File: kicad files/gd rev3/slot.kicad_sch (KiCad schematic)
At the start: 11 parts, among them J10 Apple_II_Slot, J11 Slot-Only Sigs, J12 -5V, SW2 DEV, SW3 IOSEL, U12 Slotmaker, U13 74HCT245

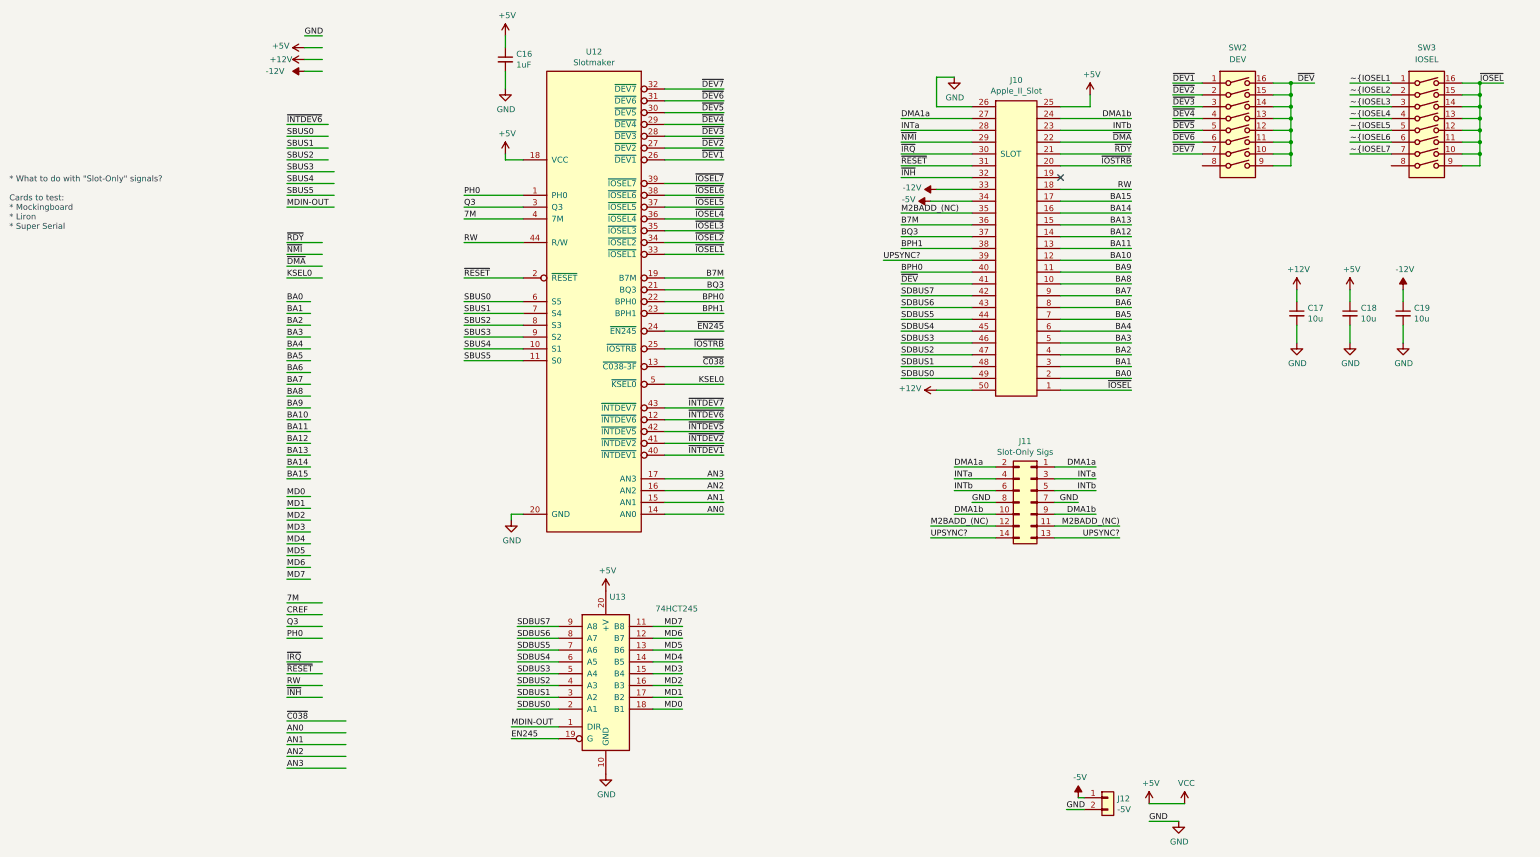
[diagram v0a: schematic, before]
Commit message: initial slot/io breakout sheet labels
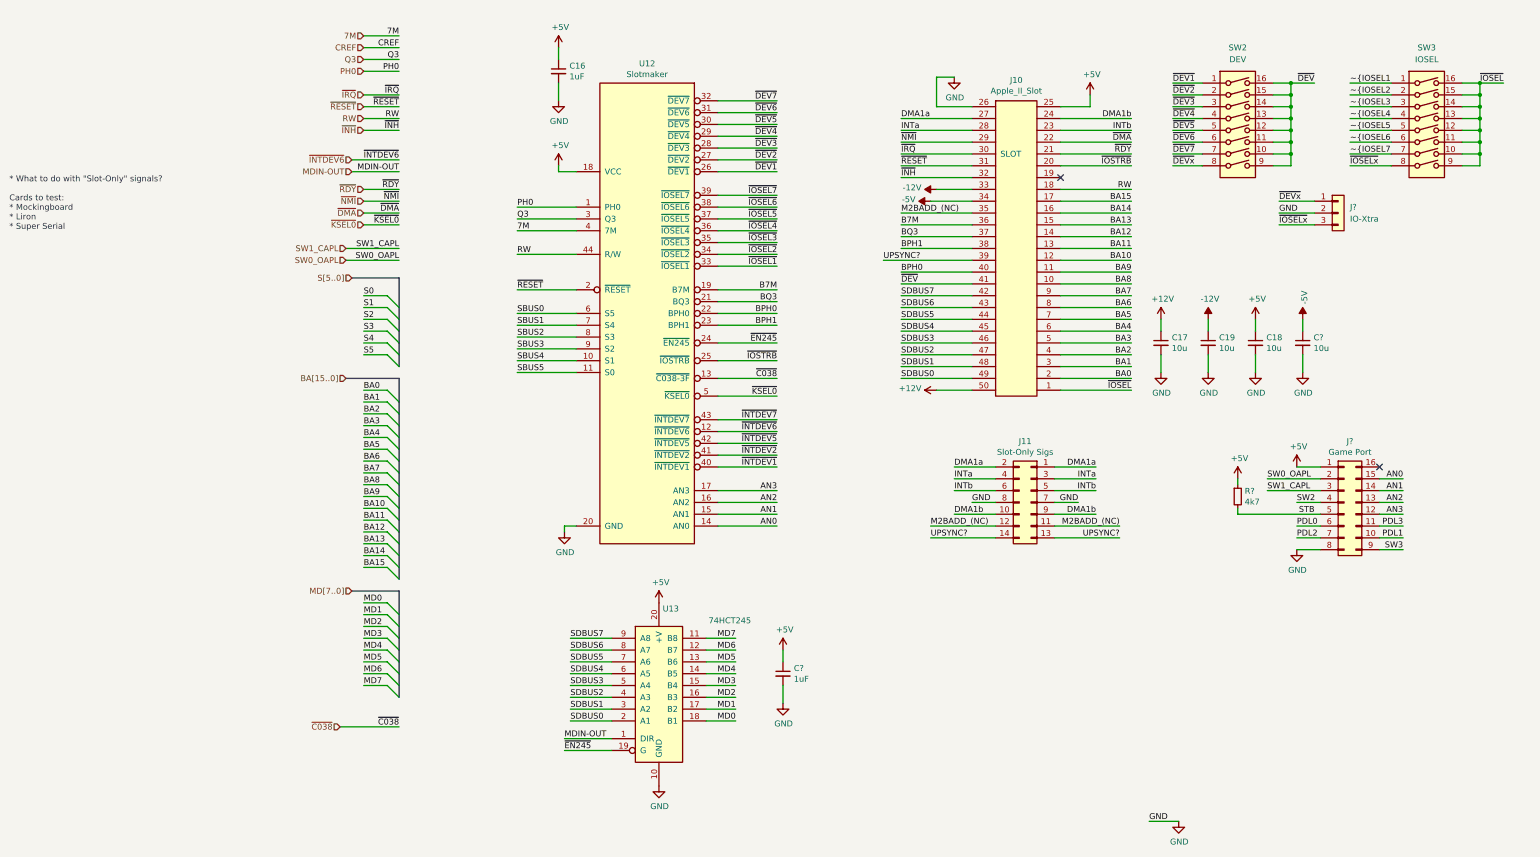
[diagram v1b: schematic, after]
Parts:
- removed J12: -5V, My Libraries:PinHeader_1x02_P2.54mm_Vertical-LOCK, symbol Connector_Generic:Conn_01x02
- added C?: 10u, Capacitor_SMD:C_0805_2012Metric, symbol My_Library:C_0805
- added C?: 1uF, Capacitor_SMD:C_0805_2012Metric, symbol My_Library:C_0805
- added J?: IO-Xtra, symbol Connector_Generic:Conn_01x03
- added J?: Game Port, Package_DIP:DIP-16_W7.62mm_Socket, symbol Connector_Generic:Conn_02x08_Counter_Clockwise
- added R?: 4k7, Resistor_SMD:R_0805_2012Metric, symbol My_Library:R_0805
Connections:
- net EN245 is gone; now on net ~{EN245}: U13.19 (G)
- net +5V: now also C?.1, J?.1 (Pin_1), R?.1
- net -5V: now also C?.1
- net AN0: now also J?.15 (Pin_15)
- net AN1: now also J?.14 (Pin_14)
- net AN2: now also J?.13 (Pin_13)
- net AN3: now also J?.12 (Pin_12)
- net GND: now also C?.2, C?.2, J?.2 (Pin_2), J?.8 (Pin_8)
- net ~{DEVx}: now reaches SW2.8
- net ~{DEVx}: now also J?.1 (Pin_1)
- net ~{IOSELx}: now reaches SW3.8
- net ~{IOSELx}: now also J?.3 (Pin_3)
- net KSEL0 renamed ~{KSEL0}
- new net PDL0: J?.6 (Pin_6)
- new net PDL1: J?.10 (Pin_10)
- new net PDL2: J?.7 (Pin_7)
- new net PDL3: J?.11 (Pin_11)
- new net STB: J?.5 (Pin_5), R?.2
- new net SW0_OAPL: J?.2 (Pin_2)
- new net SW1_CAPL: J?.3 (Pin_3)
- new net SW2: J?.4 (Pin_4)
- new net SW3: J?.9 (Pin_9)
- no-connect marks 1 -> 2
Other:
- note added: "~{}"
- title: (none) -> Slotmaker and Game DIP
- moved on the sheet: C16, C17, C18, C19, U12, U13

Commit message: update to pcb, minor updates to component placements
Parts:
- J9: renamed from J?; footprint (none) -> Connector_PinHeader_2.54mm:PinHeader_1x03_P2.54mm_Vertical
- gave numbers to parts that had none: 4
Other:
- moved on the sheet: J9
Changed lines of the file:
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@@
     (stroke (width 0) (type default) (color 0 0 0 0))
   )
-  (wire (pts (xy 231.14 60.96) (xy 238.76 60.96))
+  (wire (pts (xy 232.41 64.77) (xy 240.03 64.77))
     (stroke (width 0) (type default) (color 0 0 0 0))
   )
@@
     (stroke (width 0) (type default) (color 0 0 0 0))
   )
-  (wire (pts (xy 231.14 58.42) (xy 238.76 58.42))
+  (wire (pts (xy 232.41 62.23) (xy 240.03 62.23))
     (stroke (width 0) (type default) (color 0 0 0 0))
   )
@@
     (stroke (width 0) (type default) (color 0 0 0 0))
   )
-  (wire (pts (xy 231.14 63.5) (xy 238.76 63.5))
+  (wire (pts (xy 232.41 67.31) (xy 240.03 67.31))
     (stroke (width 0) (type default) (color 0 0 0 0))
   )
@@
     (effects (font (size 1.27 1.27)) (justify right bottom))
   )
-  (label "GND" (at 231.14 60.96 0)
+  (label "GND" (at 232.41 64.77 0)
     (effects (font (size 1.27 1.27)) (justify left bottom))
   )
@@
     (effects (font (size 1.27 1.27)) (justify left bottom))
   )
-  (label "~{IOSELx}" (at 231.14 63.5 0)
+  (label "~{IOSELx}" (at 232.41 67.31 0)
     (effects (font (size 1.27 1.27)) (justify left bottom))
   )
@@
     (effects (font (size 1.27 1.27)) (justify left bottom))
   )
-  (label "~{DEVx}" (at 231.14 58.42 0)
+  (label "~{DEVx}" (at 232.41 62.23 0)
     (effects (font (size 1.27 1.27)) (justify left bottom))
   )
@@
   (symbol (lib_id "power:GND") (at 234.95 133.35 0) (unit 1)
     (in_bom yes) (on_board yes)
-    (property "Reference" "#PWR?" (id 0) (at 234.95 139.7 0)
+    (property "Reference" "#PWR0217" (id 0) (at 234.95 139.7 0)
       (effects (font (size 1.27 1.27)) hide)
     )
@@
   (symbol (lib_id "power:+5V") (at 222.25 118.11 0) (unit 1)
     (in_bom yes) (on_board yes)
-    (property "Reference" "#PWR?" (id 0) (at 222.25 121.92 0)
+    (property "Reference" "#PWR0208" (id 0) (at 222.25 121.92 0)
       (effects (font (size 1.27 1.27)) hide)
     )
@@
   (symbol (lib_id "My_Library:C_0805") (at 236.22 88.9 0) (unit 1)
     (in_bom yes) (on_board yes)
-    (property "Reference" "C?" (id 0) (at 238.5568 87.7316 0)
+    (property "Reference" "C56" (id 0) (at 238.5568 87.7316 0)
       (effects (font (size 1.27 1.27)) (justify left))
     )
@@
     (pin "1")
   )
-  (symbol (lib_id "Connector_Generic:Conn_01x03") (at 243.84 60.96 0) (unit 1)
+  (symbol (lib_id "Connector_Generic:Conn_01x03") (at 245.11 64.77 0) (unit 1)
     (in_bom yes) (on_board yes) (fields_autoplaced)
-    (property "Reference" "J?" (id 0) (at 246.38 59.6899 0)
+    (property "Reference" "J9" (id 0) (at 247.65 63.4999 0)
       (effects (font (size 1.27 1.27)) (justify left))
     )
-    (property "Value" "IO-Xtra" (id 1) (at 246.38 62.2299 0)
+    (property "Value" "IO-Xtra" (id 1) (at 247.65 66.0399 0)
       (effects (font (size 1.27 1.27)) (justify left))
     )
-    (property "Footprint" "" (id 2) (at 243.84 60.96 0)
-      (effects (font (size 1.27 1.27)) hide)
-    )
-    (property "Datasheet" "~" (id 3) (at 243.84 60.96 0)
+    (property "Footprint" "Connector_PinHeader_2.54mm:PinHeader_1x03_P2.54mm_Vertical" (id 2) (at 245.11 64.77 0)
+      (effects (font (size 1.27 1.27)) hide)
+    )
+    (property "Datasheet" "~" (id 3) (at 245.11 64.77 0)
       (effects (font (size 1.27 1.27)) hide)
     )
@@
   (symbol (lib_id "power:GND") (at 236.22 95.25 0) (unit 1)
     (in_bom yes) (on_board yes)
-    (property "Reference" "#PWR?" (id 0) (at 236.22 101.6 0)
+    (property "Reference" "#PWR0176" (id 0) (at 236.22 101.6 0)
       (effects (font (size 1.27 1.27)) hide)
     )
@@
   (symbol (lib_id "power:+5V") (at 124.46 154.94 0) (unit 1)
     (in_bom yes) (on_board yes)
-    (property "Reference" "#PWR?" (id 0) (at 124.46 158.75 0)
+    (property "Reference" "#PWR0206" (id 0) (at 124.46 158.75 0)
       (effects (font (size 1.27 1.27)) hide)
     )
@@
   (symbol (lib_id "My_Library:C_0805") (at 124.46 160.02 0) (unit 1)
     (in_bom yes) (on_board yes)
-    (property "Reference" "C?" (id 0) (at 126.7968 158.8516 0)
+    (property "Reference" "C55" (id 0) (at 126.7968 158.8516 0)
       (effects (font (size 1.27 1.27)) (justify left))
     )
@@
   (symbol (lib_id "power:+5V") (at 234.95 115.57 0) (unit 1)
     (in_bom yes) (on_board yes)
-    (property "Reference" "#PWR?" (id 0) (at 234.95 119.38 0)
+    (property "Reference" "#PWR0209" (id 0) (at 234.95 119.38 0)
       (effects (font (size 1.27 1.27)) hide)
     )
@@
   (symbol (lib_id "My_Library:R_0805") (at 222.25 121.92 0) (unit 1)
     (in_bom yes) (on_board yes)
-    (property "Reference" "R?" (id 0) (at 223.7486 120.7516 0)
+    (property "Reference" "R20" (id 0) (at 223.7486 120.7516 0)
       (effects (font (size 1.27 1.27)) (justify left))
     )
@@
   (symbol (lib_id "power:-5V") (at 236.22 83.82 0) (unit 1)
     (in_bom yes) (on_board yes)
-    (property "Reference" "#PWR?" (id 0) (at 236.22 81.28 0)
+    (property "Reference" "#PWR0175" (id 0) (at 236.22 81.28 0)
       (effects (font (size 1.27 1.27)) hide)
     )
@@
   (symbol (lib_id "Connector_Generic:Conn_02x08_Counter_Clockwise") (at 245.11 123.19 0) (unit 1)
     (in_bom yes) (on_board yes)
-    (property "Reference" "J?" (id 0) (at 246.38 110.0582 0))
+    (property "Reference" "J12" (id 0) (at 246.38 110.0582 0))
     (property "Value" "Game Port" (id 1) (at 246.38 112.3696 0))
     (property "Footprint" "Package_DIP:DIP-16_W7.62mm_Socket" (id 2) (at 245.11 123.19 0)
@@
   (symbol (lib_id "power:GND") (at 124.46 166.37 0) (unit 1)
     (in_bom yes) (on_board yes)
-    (property "Reference" "#PWR?" (id 0) (at 124.46 172.72 0)
-      (effects (font (size 1.27 1.27)) hide)
-    )
+    (property "Reference" "#PWR0178" (id 0) (at 124.46 172.72 0)
+      (effects (font (size 1.27 1.27)) hide)
+    )

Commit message: ERC clean-up, wow, intern really messed up the symbols
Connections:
- net SBUS0 is gone; now on net S5: U12.6 (S5)
- net SBUS1 is gone; now on net S4: U12.7 (S4)
- net SBUS2 is gone; now on net S3: U12.8 (S3)
- net SBUS3 is gone; now on net S2: U12.9 (S2)
- net SBUS4 is gone; now on net S1: U12.10 (S1)
- net SBUS5 is gone; now on net S0: U12.11 (S0)
- net MDIN-OUT renamed MDI-MDO
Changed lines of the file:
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@@
-    (stroke (width 0) (type default) (color 0 0 0 0))
-  )
-  (wire (pts (xy 41.91 25.4) (xy 34.29 25.4))
     (stroke (width 0) (type default) (color 0 0 0 0))
   )
@@
     (effects (font (size 1.27 1.27)) (justify left bottom))
   )
+  (label "S1" (at 67.31 92.71 0)
+    (effects (font (size 1.27 1.27)) (justify left bottom))
+  )
   (label "MD7" (at 114.3 152.4 180)
     (effects (font (size 1.27 1.27)) (justify right bottom))
@@
     (effects (font (size 1.27 1.27)) (justify right bottom))
   )
-  (label "SBUS5" (at 67.31 95.25 0)
-    (effects (font (size 1.27 1.27)) (justify left bottom))
-  )
   (label "BA14" (at 34.29 134.62 0)
     (effects (font (size 1.27 1.27)) (justify left bottom))
@@
     (effects (font (size 1.27 1.27)) (justify right bottom))
   )
-  (label "CREF" (at 41.91 25.4 180)
-    (effects (font (size 1.27 1.27)) (justify right bottom))
-  )
   (label "SDBUS4" (at 149.86 86.36 0)
     (effects (font (size 1.27 1.27)) (justify left bottom))
@@
     (effects (font (size 1.27 1.27)) (justify right bottom))
   )
+  (label "S3" (at 67.31 87.63 0)
+    (effects (font (size 1.27 1.27)) (justify left bottom))
+  )
   (label "SDBUS6" (at 149.86 81.28 0)
     (effects (font (size 1.27 1.27)) (justify left bottom))
@@
     (effects (font (size 1.27 1.27)) (justify right bottom))
   )
+  (label "S2" (at 67.31 90.17 0)
+    (effects (font (size 1.27 1.27)) (justify left bottom))
+  )
   (label "RW" (at 41.91 40.64 180)
     (effects (font (size 1.27 1.27)) (justify right bottom))
@@
     (effects (font (size 1.27 1.27)) (justify left bottom))
   )
+  (label "S4" (at 67.31 85.09 0)
+    (effects (font (size 1.27 1.27)) (justify left bottom))
+  )
   (label "~{INTDEV6}" (at 123.19 107.95 180)
     (effects (font (size 1.27 1.27)) (justify right bottom))
@@
     (effects (font (size 1.27 1.27)) (justify right bottom))
   )
-  (label "MDIN-OUT" (at 41.91 52.07 180)
+  (label "MDI-MDO" (at 41.91 52.07 180)
     (effects (font (size 1.27 1.27)) (justify right bottom))
   )
@@
     (effects (font (size 1.27 1.27)) (justify right bottom))
   )
-  (label "MDIN-OUT" (at 77.47 173.99 0)
-    (effects (font (size 1.27 1.27)) (justify left bottom))
-  )
   (label "S2" (at 34.29 83.82 0)
     (effects (font (size 1.27 1.27)) (justify left bottom))
@@
     (effects (font (size 1.27 1.27)) (justify right bottom))
   )
-  (label "SBUS0" (at 67.31 82.55 0)
-    (effects (font (size 1.27 1.27)) (justify left bottom))
-  )
   (label "~{DEV1}" (at 208.28 33.02 0)
     (effects (font (size 1.27 1.27)) (justify left bottom))
@@
     (effects (font (size 1.27 1.27)) (justify left bottom))
   )
-  (label "SBUS3" (at 67.31 90.17 0)
-    (effects (font (size 1.27 1.27)) (justify left bottom))
-  )
   (label "~{DEVx}" (at 232.41 62.23 0)
     (effects (font (size 1.27 1.27)) (justify left bottom))
@@
     (effects (font (size 1.27 1.27)) (justify left bottom))
   )
-  (label "SBUS1" (at 67.31 85.09 0)
-    (effects (font (size 1.27 1.27)) (justify left bottom))
-  )
   (label "~{DEV}" (at 238.76 33.02 180)
     (effects (font (size 1.27 1.27)) (justify right bottom))
@@
     (effects (font (size 1.27 1.27)) (justify right bottom))
   )
+  (label "S5" (at 67.31 82.55 0)
+    (effects (font (size 1.27 1.27)) (justify left bottom))
+  )
   (label "~{INTDEV6}" (at 41.91 49.53 180)
     (effects (font (size 1.27 1.27)) (justify right bottom))
@@
     (effects (font (size 1.27 1.27)) (justify left bottom))
   )
-  (label "SBUS4" (at 67.31 92.71 0)
-    (effects (font (size 1.27 1.27)) (justify left bottom))
-  )
   (label "~{IOSTRB}" (at 199.39 50.8 180)
     (effects (font (size 1.27 1.27)) (justify right bottom))
@@
     (effects (font (size 1.27 1.27)) (justify right bottom))
   )
+  (label "MDI-MDO" (at 77.47 173.99 0)
+    (effects (font (size 1.27 1.27)) (justify left bottom))
+  )
   (label "~{IOSEL5" (at 246.38 43.18 0)
     (effects (font (size 1.27 1.27)) (justify left bottom))
@@
     (effects (font (size 1.27 1.27)) (justify left bottom))
   )
+  (label "S0" (at 67.31 95.25 0)
+    (effects (font (size 1.27 1.27)) (justify left bottom))
+  )
   (label "MD3" (at 34.29 152.4 0)
     (effects (font (size 1.27 1.27)) (justify left bottom))
@@
   (label "MD5" (at 114.3 157.48 180)
     (effects (font (size 1.27 1.27)) (justify right bottom))
-  )
-  (label "SBUS2" (at 67.31 87.63 0)
-    (effects (font (size 1.27 1.27)) (justify left bottom))
   )
   (label "~{IOSEL6" (at 246.38 45.72 0)
@@
     (effects (font (size 1.27 1.27)) (justify right))
   )
-  (hierarchical_label "MDIN-OUT" (shape input) (at 31.75 52.07 180)
+  (hierarchical_label "MDI-MDO" (shape input) (at 31.75 52.07 180)
     (effects (font (size 1.27 1.27)) (justify right))
   )
@@
     (effects (font (size 1.27 1.27)) (justify right))
   )
-  (hierarchical_label "CREF" (shape input) (at 34.29 25.4 180)
-    (effects (font (size 1.27 1.27)) (justify right))
-  )

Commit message: added missing Flash to 2040 circuits and sync'd title blocks
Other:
- company: (none) -> twitch.tv/baldengineer
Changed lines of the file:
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@@
   (title_block
     (title "Slotmaker and Game DIP")
-    (rev "Rev 3")
+    (rev "3a")
+    (company "twitch.tv/baldengineer")
   )
   (junction (at 233.68 33.02) (diameter 0) (color 0 0 0 0)

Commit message: on-stream clean-up work
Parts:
- removed J11: Slot-Only Sigs, Connector_PinSocket_2.54mm:PinSocket_2x07_P2.54mm_Vertical, symbol Connector_Generic:Conn_02x07_Odd_Even
- removed J12: Game Port, Package_DIP:DIP-16_W7.62mm_Socket, symbol Connector_Generic:Conn_02x08_Counter_Clockwise
- removed R20: 4k7, Resistor_SMD:R_0805_2012Metric, symbol My_Library:R_0805
- added TP16, TP17, TP4, TP5, TP6, TP7, TP8, TP9: TestPoint, TestPoint:TestPoint_Pad_D1.0mm, symbol Connector:TestPoint
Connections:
- net DMA1a: now also TP4.1
- net DMA1b: now also TP7.1
- net INTa: now also TP5.1
- net INTb: now also TP6.1
- net M2BADD_(NC): now also TP8.1
- net UPSYNC?: now also TP9.1
- net ~{C038}: now also TP16.1
- net ~{KSEL0}: now also TP17.1
- no-connect marks 2 -> 1
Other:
- note added: "C038-C03F is for IIgs SCC (Sound)"
- moved on the sheet: C17, C18, C19, C56, J10, J9, SW2, SW3

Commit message: ERC clean-up
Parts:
- added C78, C79: 1u, Capacitor_SMD:C_0603_1608Metric, symbol My_Library:C_0805
- added U32: LM7905_TO220, Package_TO_SOT_THT:TO-220-3_Vertical, symbol Regulator_Linear:LM7905_TO220
- U13: footprint Package_SO:SO-20_12.8x7.5mm_P1.27mm -> Package_SO:SOIC-20W_7.5x12.8mm_P1.27mm; symbol Apple_IIgs_Symbols:74HCT245 -> My Library:74HCT245_1
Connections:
- net -12V: now also C78.1, U32.2 (VI)
- net -5V: now also C79.1, U32.3 (VO)
- net GND: now also C78.2, C79.2, U32.1 (GND)
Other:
- note removed: "* What to do with "Slot-Only" signals? Cards to test: * Mockingboard * Liron * Super Serial"
- moved on the sheet: C16, C17, C18, C19, C55, C56, J9, SW2, SW3, TP16, TP17, TP4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

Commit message: main grouping done now optimizing groups and locations
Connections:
- net ~{DEV1}: now also SW2.7; no longer SW2.1
- net ~{DEV2}: now also SW2.6; no longer SW2.2
- net ~{DEV3}: now also SW2.5; no longer SW2.3
- net ~{DEV5}: now also SW2.3; no longer SW2.5
- net ~{DEV6}: now also SW2.2; no longer SW2.6
- net ~{DEV7}: now also SW2.1; no longer SW2.7
- net ~{IOSEL1: now also SW3.7; no longer SW3.1
- net ~{IOSEL2: now also SW3.6; no longer SW3.2
- net ~{IOSEL3: now also SW3.5; no longer SW3.3
- net ~{IOSEL5: now also SW3.3; no longer SW3.5
- net ~{IOSEL6: now also SW3.2; no longer SW3.6
- net ~{IOSEL7: now also SW3.1; no longer SW3.7
- net UPSYNC? renamed SYNC_6502

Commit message: iwm/slot rough routing
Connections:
- net ~{DEV1}: now also SW2.1; no longer SW2.7
- net ~{DEV2}: now also SW2.2; no longer SW2.6
- net ~{DEV3}: now also SW2.3; no longer SW2.5
- net ~{DEV5}: now also SW2.5; no longer SW2.3
- net ~{DEV6}: now also SW2.6; no longer SW2.2
- net ~{DEV7}: now also SW2.7; no longer SW2.1
- net ~{IOSEL1: now also SW3.1; no longer SW3.7
- net ~{IOSEL2: now also SW3.2; no longer SW3.6
- net ~{IOSEL3: now also SW3.3; no longer SW3.5
- net ~{IOSEL5: now also SW3.5; no longer SW3.3
- net ~{IOSEL6: now also SW3.6; no longer SW3.2
- net ~{IOSEL7: now also SW3.7; no longer SW3.1
